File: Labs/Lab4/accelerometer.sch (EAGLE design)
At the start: 15 parts

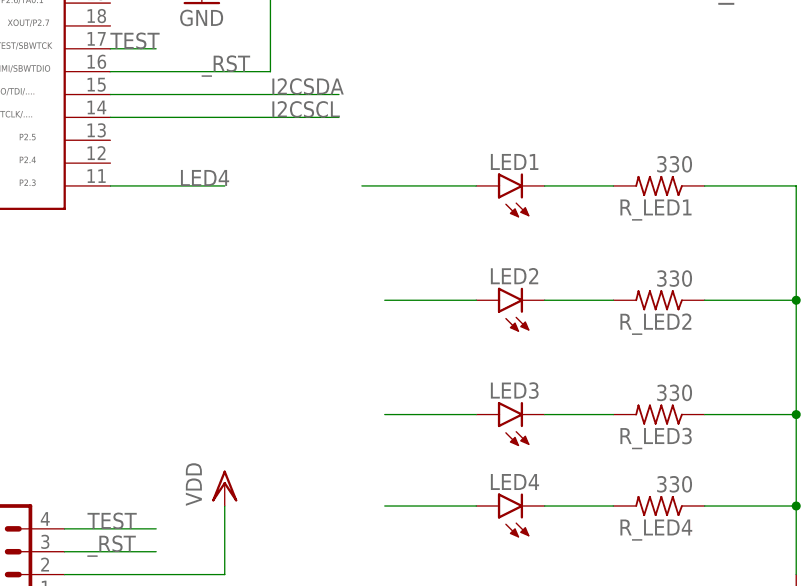
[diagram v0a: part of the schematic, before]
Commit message: Fixed connections in Lab 4 schematic
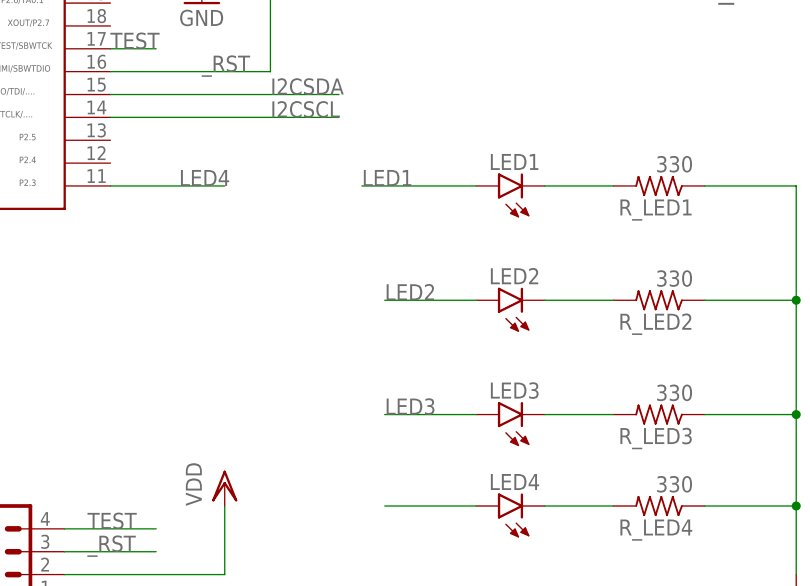
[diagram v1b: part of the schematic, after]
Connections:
- removed net N$5: LED1.A
- removed net N$6: LED2.A
- removed net N$7: LED3.A
- removed net N$8: LED4.A
- net LED1: now also LED1.A
- net LED2: now also LED2.A
- net LED3: now also LED3.A
- net LED4: now also LED4.A
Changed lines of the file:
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@@
-</segment>
-</net>
-<net name="N$5" class="0">
-<segment>
-<pinref part="LED1" gate="G$1" pin="A"/>
-<wire x1="40.64" y1="157.48" x2="27.94" y2="157.48" width="0.1524" layer="91"/>
-</segment>
-</net>
-<net name="N$6" class="0">
-<segment>
-<pinref part="LED2" gate="G$1" pin="A"/>
-<wire x1="40.64" y1="144.78" x2="30.48" y2="144.78" width="0.1524" layer="91"/>
-</segment>
-</net>
-<net name="N$7" class="0">
-<segment>
-<pinref part="LED3" gate="G$1" pin="A"/>
-<wire x1="40.64" y1="132.08" x2="30.48" y2="132.08" width="0.1524" layer="91"/>
-</segment>
-</net>
-<net name="N$8" class="0">
-<segment>
-<pinref part="LED4" gate="G$1" pin="A"/>
-<wire x1="40.64" y1="121.92" x2="30.48" y2="121.92" width="0.1524" layer="91"/>
 </segment>
 </net>
@@
 <label x="-60.96" y="162.56" size="1.778" layer="95"/>
 </segment>
+<segment>
+<pinref part="LED1" gate="G$1" pin="A"/>
+<wire x1="40.64" y1="157.48" x2="27.94" y2="157.48" width="0.1524" layer="91"/>
+<label x="27.94" y="157.48" size="1.778" layer="95"/>
+</segment>
 </net>
 <net name="LED2" class="0">
@@
 <wire x1="-48.26" y1="160.02" x2="-60.96" y2="160.02" width="0.1524" layer="91"/>
 <label x="-60.96" y="160.02" size="1.778" layer="95"/>
+</segment>
+<segment>
+<pinref part="LED2" gate="G$1" pin="A"/>
+<wire x1="40.64" y1="144.78" x2="30.48" y2="144.78" width="0.1524" layer="91"/>
+<label x="30.48" y="144.78" size="1.778" layer="95"/>
 </segment>
 </net>
@@
 <label x="-60.96" y="157.48" size="1.778" layer="95"/>
 </segment>
+<segment>
+<pinref part="LED3" gate="G$1" pin="A"/>
+<wire x1="40.64" y1="132.08" x2="30.48" y2="132.08" width="0.1524" layer="91"/>
+<label x="30.48" y="132.08" size="1.778" layer="95"/>
+</segment>
 </net>
 <net name="LED4" class="0">
@@
 <label x="7.62" y="157.48" size="1.778" layer="95"/>
 </segment>
+<segment>
+<pinref part="LED4" gate="G$1" pin="A"/>
+<wire x1="40.64" y1="121.92" x2="30.48" y2="121.92" width="0.1524" layer="91"/>
+</segment>
 </net>
